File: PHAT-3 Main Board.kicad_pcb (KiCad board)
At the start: 6 copper layers, 95.9 x 90.2 mm, 34 parts, among them P1 Power Terminal Block, P2 Power Terminal Block, P3 Power Terminal Block, P4 Power Terminal Block, Q1 IRLZ44N, SW1 SW_Push_SPDT, U1 AHT21, U10 Logic Level Converter, U2 ESP32-S3 Dual-core SX1262, U3 GY-68 BMP180, U4 GY-521 MPU-6050, U5 LM2596, U6 GT-7U, U7 SCD41, U8 uCAM-III, U9 SDHC

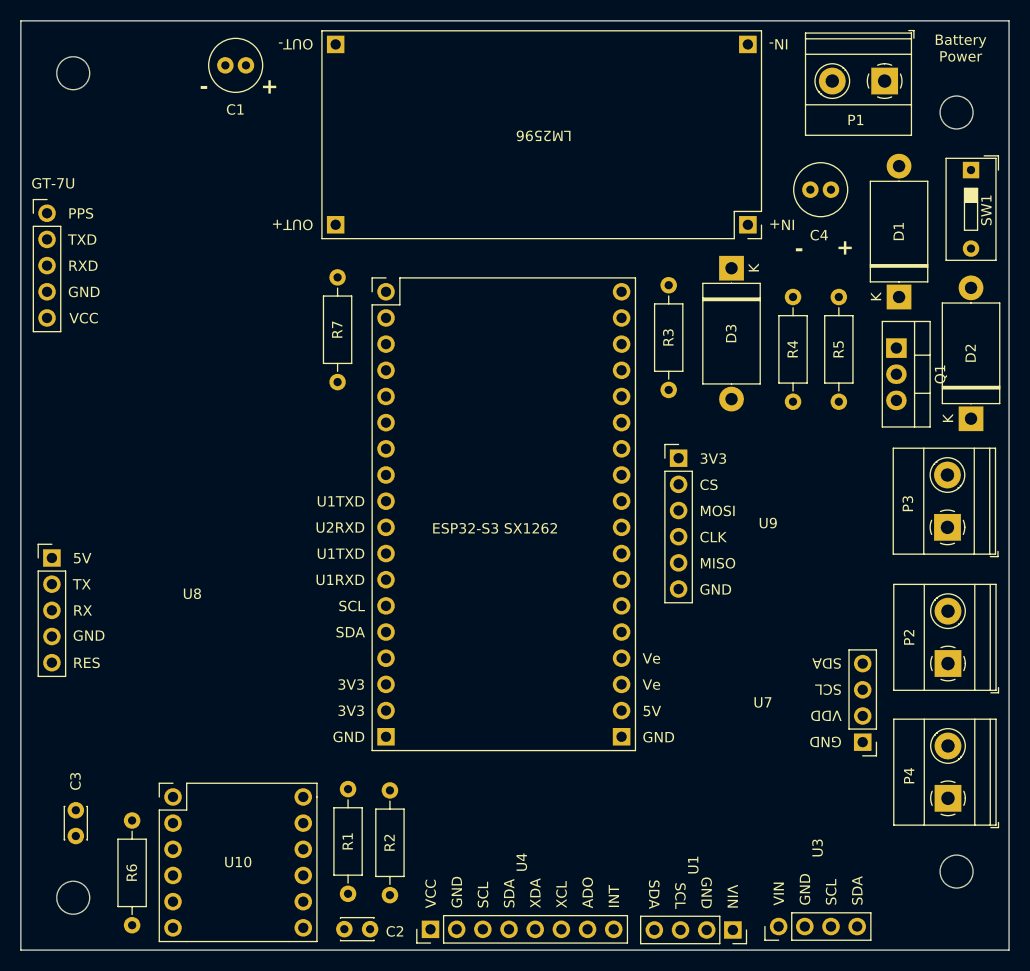
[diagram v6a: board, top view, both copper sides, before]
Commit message: Updated Switch and Resistor Placement
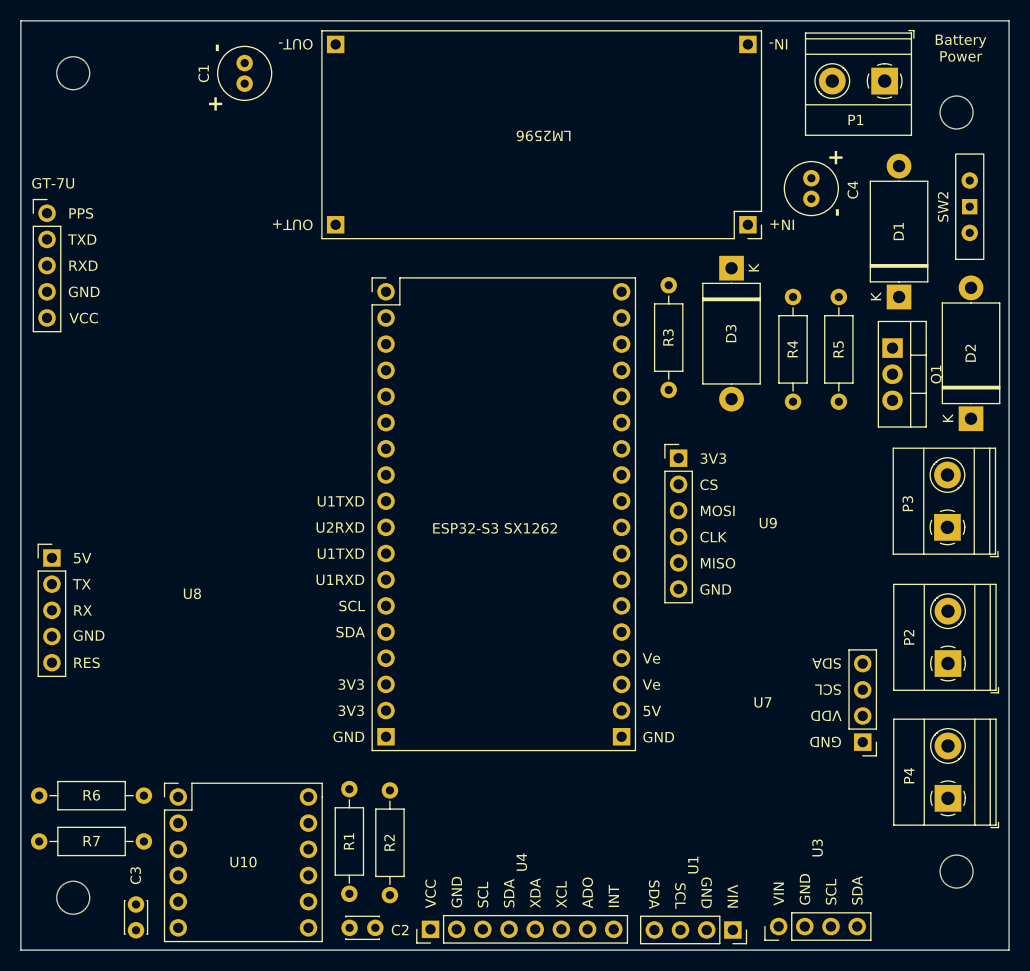
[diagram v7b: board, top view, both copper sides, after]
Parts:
- removed SW1: SW_Push_SPDT, Button_Switch_THT:SW_DIP_SPSTx01_Slide_9.78x4.72mm_W7.62mm_P2.54mm
- added SW2: SW_DPDT_x2, Button_Switch_THT:SW_Slide-03_Wuerth-WS-SLTV_10x2.5x6.4_P2.54mm, F.Cu at (188.6, 63.8)
- moved R7 57.9 mm to (108.5, 125.3), turned to 180 degrees
- moved C3 10.9 mm to (107.7, 131.5)
- moved R6 9.33 mm to (98.3, 120.9), turned to 0 degrees
- moved C1 2.58 mm to (118.2, 51.8), turned to 90 degrees
- moved C4 0.89 mm to (173.2, 63.0), turned to 90 degrees
- moved C2 0.52 mm to (128.4, 133.7)
- moved U10 0.51 mm to (111.8, 121.0)
- moved Q1 0.38 mm to (181.1, 77.5)
- moved R1 0.13 mm to (128.4, 130.4)
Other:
- board text added: "Designed by Yehoshua Luna with kind help from Marcin Anforowicz and Evan Gubarev. https://github.com/UWCubeSat/PHAT-3-Main-Board"

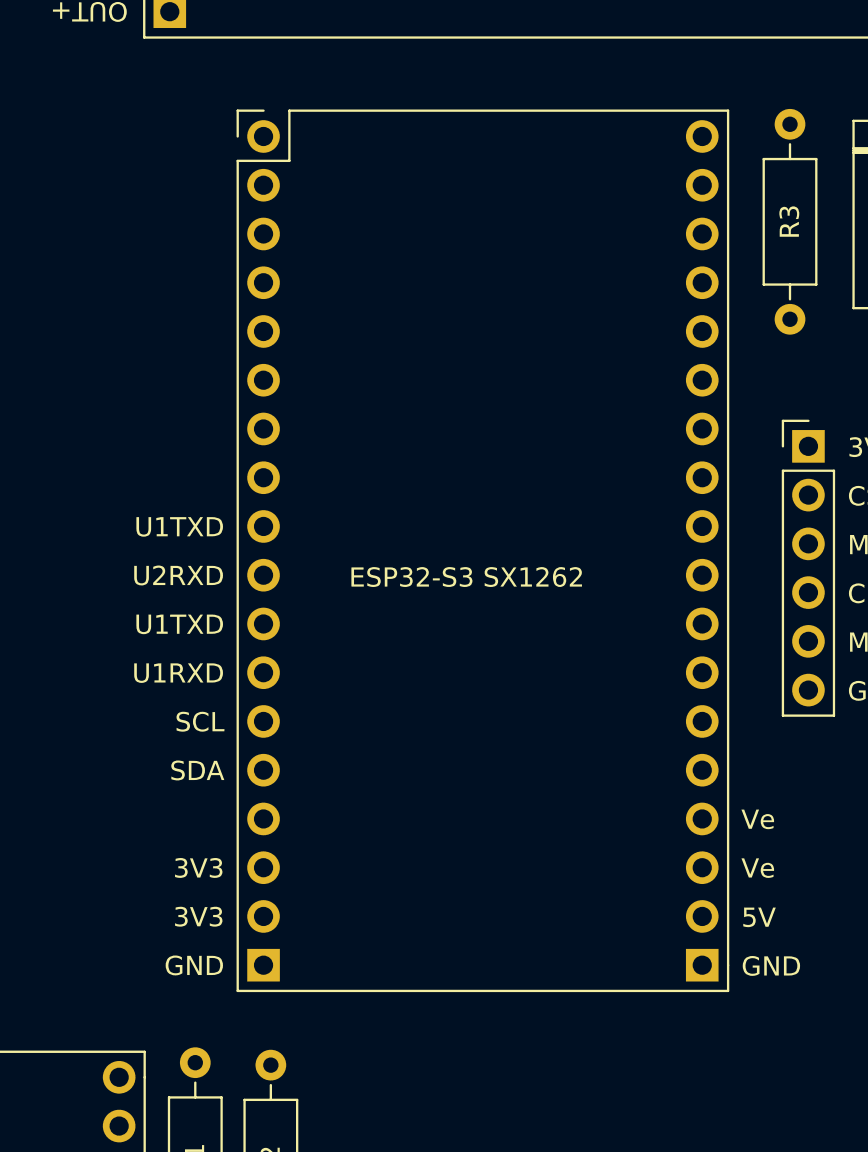
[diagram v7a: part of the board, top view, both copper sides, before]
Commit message: Changed UART and I2C Pins
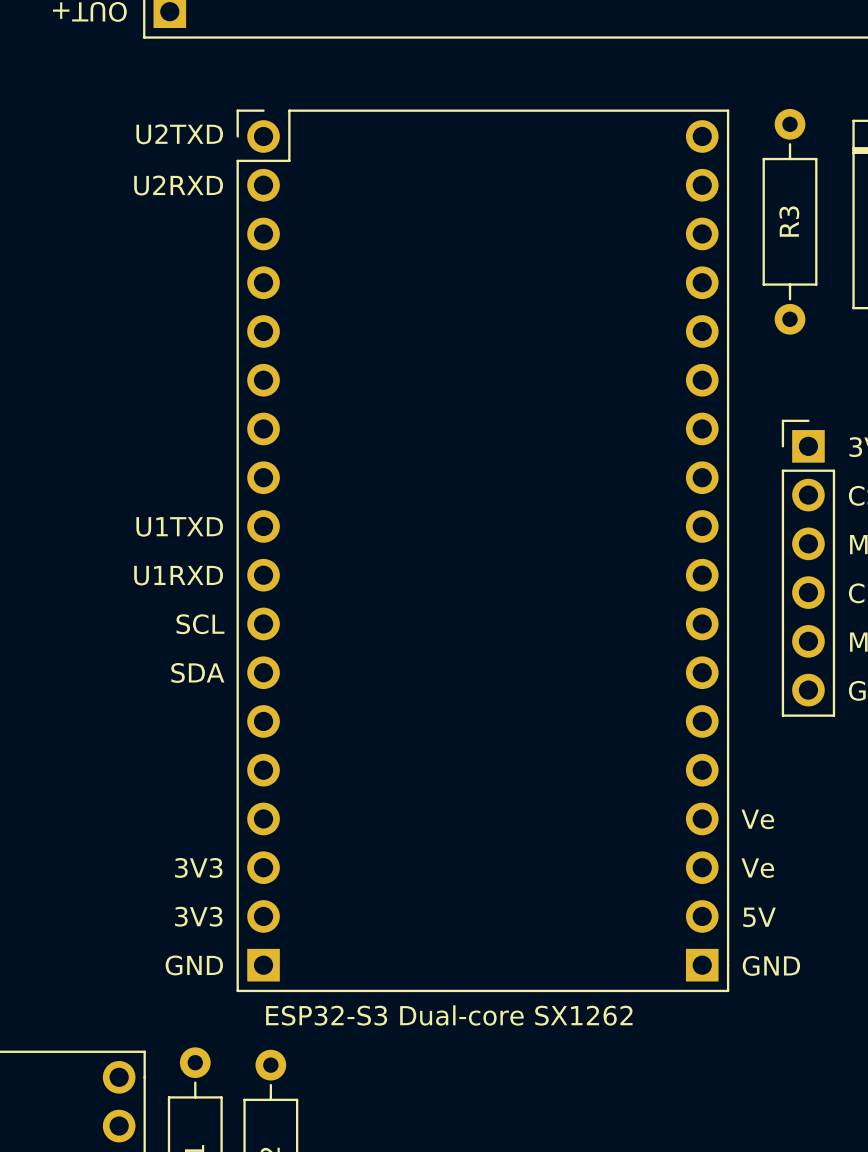
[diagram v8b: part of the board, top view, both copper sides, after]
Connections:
- U2 pad 1: unconnected-(U2-DATA-Pad1) -> Net-(U6-RXD)
- U2 pad 11: Net-(U2-U1TXD) -> Net-(U1-SCL)
- U2 pad 12: Net-(U2-U1RXD) -> Net-(U1-SDA)
- U2 pad 13: Net-(U1-SCL) -> unconnected-(U2-SCL-Pad13)
- U2 pad 14: Net-(U1-SDA) -> unconnected-(U2-SDA-Pad14)
- U2 pad 2: unconnected-(U2-DATA-Pad2) -> Net-(U6-TXD)
- U6 pad 2: Net-(U2-U2RXD) -> Net-(U6-TXD)
- U6 pad 3: Net-(U2-U2TXD) -> Net-(U6-RXD)
- U8 pad 2: Net-(U2-U1RXD) -> Net-(U2-U2RXD)
- U8 pad 3: Net-(U2-U1TXD) -> Net-(U2-U2TXD)
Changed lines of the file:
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@@
 	(net 14 "unconnected-(U2-DATA-Pad26)")
 	(net 15 "unconnected-(U2-ADC_CTRL-Pad15)")
-	(net 16 "unconnected-(U2-DATA-Pad2)")
+	(net 16 "Net-(U6-RXD)")
 	(net 17 "unconnected-(U2-U0TXD-Pad24)")
 	(net 18 "Net-(U10-HV1)")
@@
 	(net 26 "Net-(U2-HTR)")
 	(net 27 "unconnected-(U2-DATA-Pad34)")
-	(net 28 "Net-(U2-U1RXD)")
+	(net 28 "unconnected-(U2-SCL-Pad13)")
 	(net 29 "+3V3")
 	(net 30 "unconnected-(U2-3V3-Pad16)")
@@
 	(net 35 "Net-(U2-U2RXD)")
 	(net 36 "unconnected-(U2-DATA-Pad33)")
-	(net 37 "Net-(U2-U1TXD)")
-	(net 38 "unconnected-(U2-DATA-Pad1)")
+	(net 37 "unconnected-(U2-SDA-Pad14)")
+	(net 38 "Net-(U6-TXD)")
 	(net 39 "unconnected-(U4-XDA-Pad5)")
 	(net 40 "unconnected-(U4-ADO-Pad7)")
@@
 		(tags "Resistor Axial_DIN0207 series Axial Horizontal pin pitch 10.16mm 0.25W = 1/4W length 6.3mm diameter 2.5mm")
 		(property "Reference" "R6"
-			(at 5.08 0 360)
+			(at 5.08 0 0)
 			(layer "F.SilkS")
 			(effects
@@
 		)
 		(property "Value" "10k"
-			(at 5.08 2.37 360)
+			(at 5.08 2.37 0)
 			(layer "F.Fab")
 			(effects
@@
 		)
 		(fp_text user "${REFERENCE}"
-			(at 5.08 0 360)
+			(at 5.08 0 0)
 			(layer "F.Fab")
 			(effects
@@
 			(layers "*.Cu" "*.Mask")
 			(remove_unused_layers no)
-			(net 28 "Net-(U2-U1RXD)")
+			(net 35 "Net-(U2-U2RXD)")
 			(pinfunction "TX")
 			(pintype "bidirectional")
@@
 			(layers "*.Cu" "*.Mask")
 			(remove_unused_layers no)
-			(net 37 "Net-(U2-U1TXD)")
+			(net 10 "Net-(U2-U2TXD)")
 			(pinfunction "RX")
 			(pintype "bidirectional")
@@
 			(layers "*.Cu" "*.Mask")
 			(remove_unused_layers no)
-			(net 35 "Net-(U2-U2RXD)")
+			(net 38 "Net-(U6-TXD)")
 			(pinfunction "TXD")
 			(pintype "bidirectional")
@@
 			(layers "*.Cu" "*.Mask")
 			(remove_unused_layers no)
-			(net 10 "Net-(U2-U2TXD)")
+			(net 16 "Net-(U6-RXD)")
 			(pinfunction "RXD")
 			(pintype "bidirectional")
@@
 			(layer "F.Fab")
 		)
-		(fp_text user "GND"
-			(at -2.032 43.815 0)
+		(fp_text user "U2RXD"
+			(at -2.032 3.175 0)
 			(unlocked yes)
 			(layer "F.SilkS")
@@
 			)
 		)
-		(fp_text user "SDA"
-			(at -2.032 33.655 0)
+		(fp_text user "Ve"
+			(at 24.892 38.735 0)
 			(unlocked yes)
 			(layer "F.SilkS")
@@
 					(thickness 0.15)
 				)
-				(justify right bottom)
+				(justify left bottom)
 			)
 		)
-		(fp_text user "U1RXD"
-			(at -2.032 28.575 0)
+		(fp_text user "SCL"
+			(at -2.032 26.035 0)
 			(unlocked yes)
 			(layer "F.SilkS")
@@
 			)
 		)
-		(fp_text user "SCL"
-			(at -2.032 31.115 0)
+		(fp_text user "Ve"
+			(at 24.892 36.195 0)
 			(unlocked yes)
 			(layer "F.SilkS")
@@
 					(thickness 0.15)
 				)
-				(justify right bottom)
+				(justify left bottom)
 			)
 		)
-		(fp_text user "U2RXD"
-			(at -2.032 23.495 0)
+		(fp_text user "U2TXD"
+			(at -2.032 0.508 0)
 			(unlocked yes)
 			(layer "F.SilkS")
@@
 			)
 		)
-		(fp_text user "Ve"
-			(at 24.892 36.195 0)
+		(fp_text user "3V3"
+			(at -2.032 38.735 0)
 			(unlocked yes)
 			(layer "F.SilkS")
@@
 					(thickness 0.15)
 				)
-				(justify left bottom)
+				(justify right bottom)
 			)
 		)
-		(fp_text user "ESP32-S3 SX1262"
-			(at 4.445 23.576 0)
+		(fp_text user "3V3"
+			(at -2.032 41.275 0)
 			(unlocked yes)
 			(layer "F.SilkS")
@@
 					(thickness 0.15)
 				)
-				(justify left bottom)
+				(justify right bottom)
 			)
 		)
-		(fp_text user "Ve"
-			(at 24.892 38.735 0)
+		(fp_text user "5V"
+			(at 24.892 41.3004 0)
 			(unlocked yes)
 			(layer "F.SilkS")
@@
 			)
 		)
-		(fp_text user "3V3"
-			(at -2.032 38.735 0)
+		(fp_text user "GND"
+			(at 24.892 43.8404 0)
 			(unlocked yes)
 			(layer "F.SilkS")
@@
 					(thickness 0.15)
 				)
-				(justify right bottom)
+				(justify left bottom)
 			)
 		)
-		(fp_text user "3V3"
-			(at -2.032 41.275 0)
+		(fp_text user "GND"
+			(at -2.032 43.815 0)
 			(unlocked yes)
 			(layer "F.SilkS")
@@
 			)
 		)
-		(fp_text user "GND"
-			(at 24.892 43.8404 0)
+		(fp_text user "ESP32-S3 Dual-core SX1262"
+			(at 0 46.4312 0)
 			(unlocked yes)
 			(layer "F.SilkS")
@@
 			)
 		)
-		(fp_text user "5V"
-			(at 24.892 41.3004 0)
+		(fp_text user "SDA"
+			(at -2.032 28.575 0)
 			(unlocked yes)
 			(layer "F.SilkS")
@@
 					(thickness 0.15)
 				)
-				(justify left bottom)
+				(justify right bottom)
 			)
 		)
-		(fp_text user "U1TXD"
-			(at -2.032 26.035 0)
+		(fp_text user "U1RXD"
+			(at -2.032 23.495 0)
 			(unlocked yes)
 			(layer "F.SilkS")
@@
 			(layers "*.Cu" "*.Mask")
 			(remove_unused_layers no)
-			(net 38 "unconnected-(U2-DATA-Pad1)")
+			(net 16 "Net-(U6-RXD)")
 			(pinfunction "DATA")
-			(pintype "bidirectional+no_connect")
+			(pintype "bidirectional")
 		)
 		(pad "2" thru_hole oval
@@
 			(layers "*.Cu" "*.Mask")
 			(remove_unused_layers no)
-			(net 16 "unconnected-(U2-DATA-Pad2)")
+			(net 38 "Net-(U6-TXD)")
 			(pinfunction "DATA")
-			(pintype "bidirectional+no_connect")
+			(pintype "bidirectional")
 		)
 		(pad "3" thru_hole oval
@@
 			(layers "*.Cu" "*.Mask")
 			(remove_unused_layers no)
-			(net 37 "Net-(U2-U1TXD)")
+			(net 6 "Net-(U1-SCL)")
 			(pinfunction "U1TXD")
 			(pintype "bidirectional")
@@
 			(layers "*.Cu" "*.Mask")
 			(remove_unused_layers no)
-			(net 28 "Net-(U2-U1RXD)")
+			(net 5 "Net-(U1-SDA)")
 			(pinfunction "U1RXD")
 			(pintype "bidirectional")
@@
 			(layers "*.Cu" "*.Mask")
 			(remove_unused_layers no)
-			(net 6 "Net-(U1-SCL)")
+			(net 28 "unconnected-(U2-SCL-Pad13)")
 			(pinfunction "SCL")
-			(pintype "bidirectional")
+			(pintype "bidirectional+no_connect")
 		)
 		(pad "14" thru_hole oval
@@
 			(layers "*.Cu" "*.Mask")
 			(remove_unused_layers no)
-			(net 5 "Net-(U1-SDA)")
+			(net 37 "unconnected-(U2-SDA-Pad14)")
 			(pinfunction "SDA")
-			(pintype "bidirectional")
+			(pintype "bidirectional+no_connect")
 		)
 		(pad "15" thru_hole oval
